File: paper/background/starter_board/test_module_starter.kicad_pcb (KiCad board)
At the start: 2 copper layers, 82.3 x 112.9 mm, 14 parts, among them J1 Barrel_Jack_12V, M1 ERM_Motor, M2 Stepper_4wire, M3 Servo_3pin, U1 D24V22F5_Buck, U2 Pi_Pico_W, U3 DRV2605L_Breakout, U4 DRV8871_Breakout, U5 Tic_T500

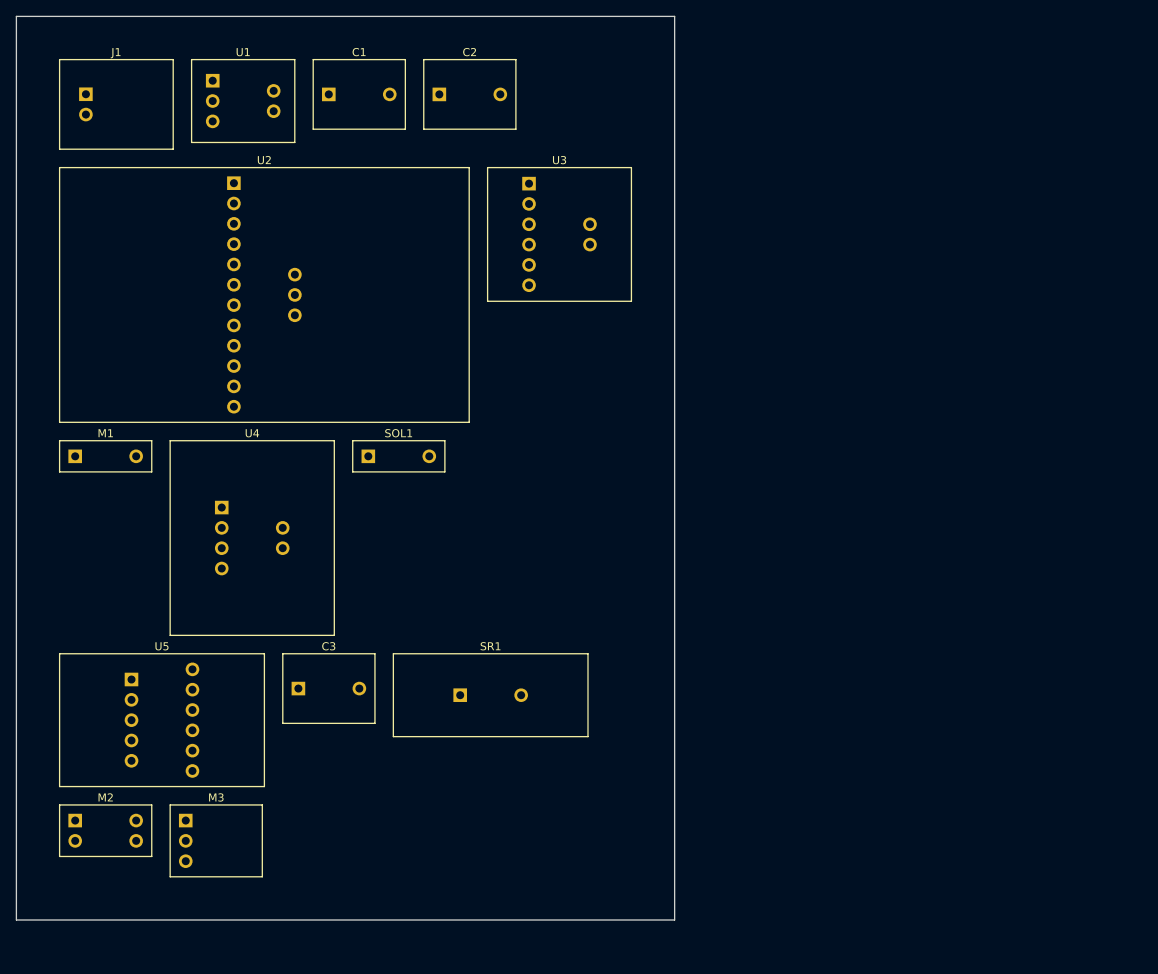
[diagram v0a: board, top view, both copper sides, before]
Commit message: Fix starter-board pin counts to match real parts (Pico W 15→40, etc.)
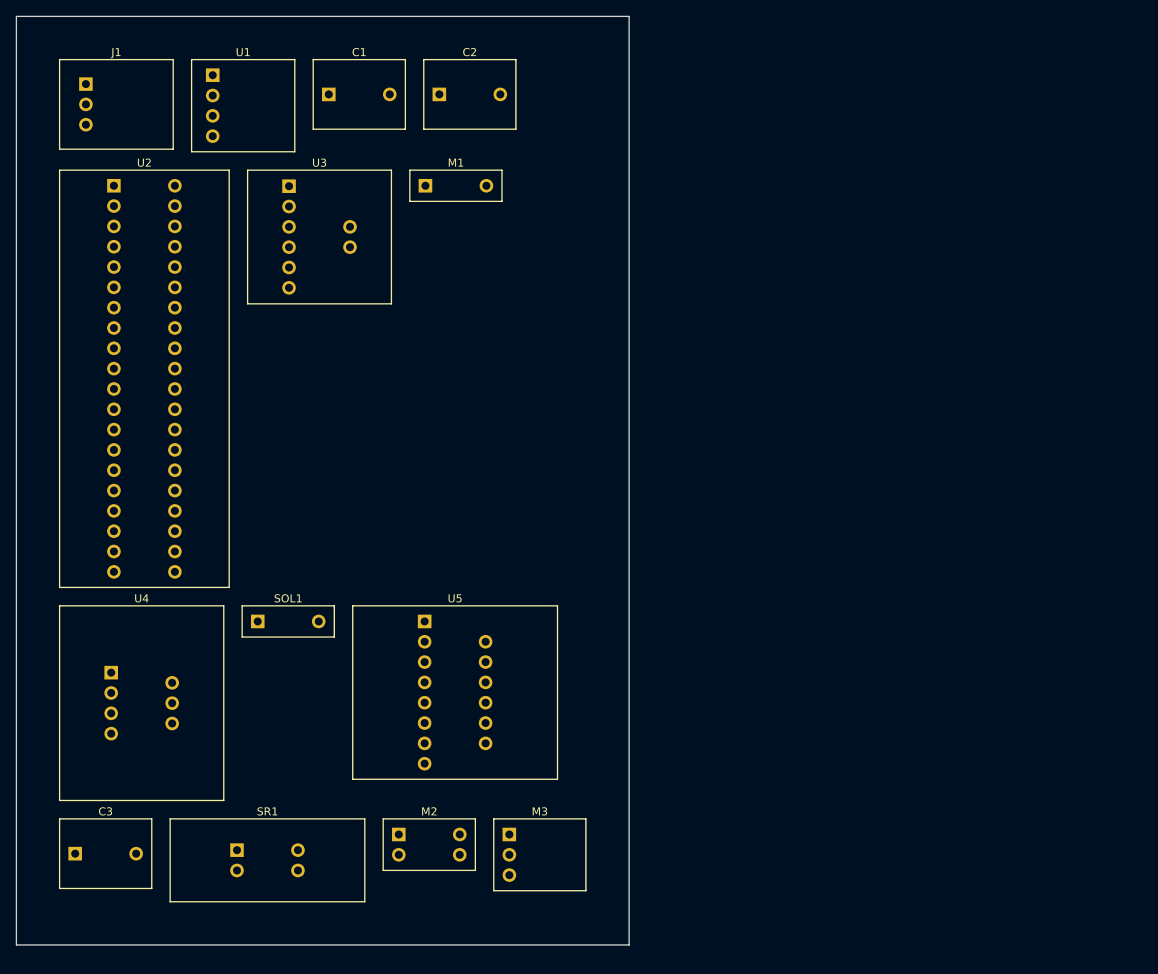
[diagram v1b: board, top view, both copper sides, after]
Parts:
- moved M1 55.3 mm to (49.9, 16.2)
- moved M2 40.5 mm to (46.6, 98.5)
- moved M3 40.5 mm to (60.4, 99.8)
- moved U5 36.8 mm to (49.8, 79.5)
- moved C3 34.7 mm to (6.16, 99.7)
- moved SR1 34.7 mm to (26.4, 100.5)
- moved U3 30.0 mm to (32.9, 22.6)
- moved U4 24.8 mm to (10.7, 80.8)
- moved SOL1 24.8 mm to (29.0, 70.6)
- moved U2 18.3 mm to (11.0, 40.3)
- moved U1 0.58 mm to (23.4, 6.16)
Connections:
- SR1 pad 2: GND -> +12V
- U1 pad 3: +12V -> +5V
- U1 pad 4: +5V -> +12V
- U2 pad 10: SOL_IN2 -> (no net)
- U2 pad 11: HAPT_EN -> (no net)
- U2 pad 12: SERVO_SIG -> (no net)
- U2 pad 13: +5V -> GND
- U2 pad 14: GND -> SOL_IN1
- U2 pad 15: +3V3 -> SOL_IN2
- U2 pad 3: (no net) -> GND
- U2 pad 5: STP_TX -> (no net)
- U2 pad 6: STP_RX -> STP_TX
- U2 pad 7: (no net) -> STP_RX
- U2 pad 8: (no net) -> GND
- U2 pad 9: SOL_IN1 -> (no net)
- U4 pad 3: SOL_IN1 -> SOL_A
- U4 pad 4: SOL_IN2 -> SOL_B
- U4 pad 5: SOL_A -> SOL_IN1
- U4 pad 6: SOL_B -> SOL_IN2
- U5 pad 10: STP_B1 -> GND
- U5 pad 11: STP_B2 -> STP_A1
- U5 pad 6: +12V -> (no net)
- U5 pad 8: STP_A1 -> (no net)
- U5 pad 9: STP_A2 -> +12V
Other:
- board size 82.3 x 112.9 mm -> 76.6 x 116.1 mm

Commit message: Swap starter-board placeholder pads for real KiCad library footprints
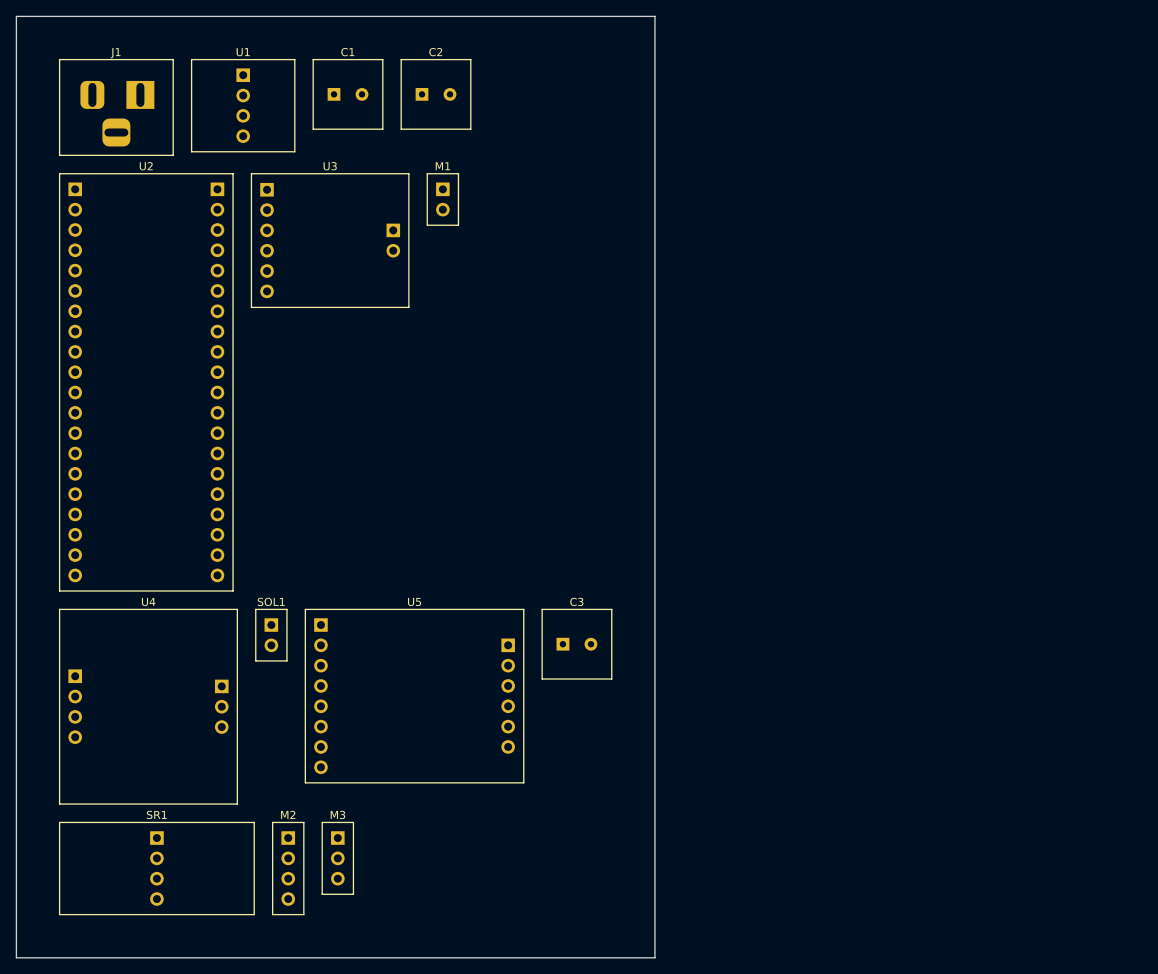
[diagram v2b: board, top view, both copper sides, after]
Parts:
- C1, C2, C3: footprint powder_doser_parts:Cap_Polar -> Capacitor_THT:CP_Radial_D8.0mm_P3.50mm
- J1: footprint powder_doser_parts:Barrel_Jack_12V -> Connector_BarrelJack:BarrelJack_Horizontal
- M1: footprint powder_doser_parts:ERM_Motor -> Connector_PinHeader_2.54mm:PinHeader_1x02_P2.54mm_Vertical
- M2: footprint powder_doser_parts:Stepper_4wire -> Connector_PinHeader_2.54mm:PinHeader_1x04_P2.54mm_Vertical
- M3: footprint powder_doser_parts:Servo_3pin -> Connector_PinHeader_2.54mm:PinHeader_1x03_P2.54mm_Vertical
- SOL1: footprint powder_doser_parts:Solenoid -> Connector_PinHeader_2.54mm:PinHeader_1x02_P2.54mm_Vertical
- moved C3 64.5 mm to (65.1, 73.5)
- moved M3 25.3 mm to (35.2, 100.2)
- moved M2 17.9 mm to (29.0, 101.5)
- moved SR1 13.9 mm to (12.6, 101.5)
- moved U5 5.09 mm to (44.8, 80.0)
- moved C2 4.23 mm to (47.5, 4.75)
- moved SOL1 2.72 mm to (26.9, 72.3)
- moved M1 2.37 mm to (48.3, 17.9)
- moved C1 1.41 mm to (36.5, 4.75)
- moved U3 1.40 mm to (34.2, 23.0)
- moved U4 0.96 mm to (11.5, 81.3)
- moved U2 0.51 mm to (11.2, 40.7)
- moved J1 0.38 mm to (7.50, 6.38)
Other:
- board size 76.6 x 116.1 mm -> 79.8 x 117.7 mm

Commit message: Implement Edison feedback: domain/cluster/edge-aware board placement
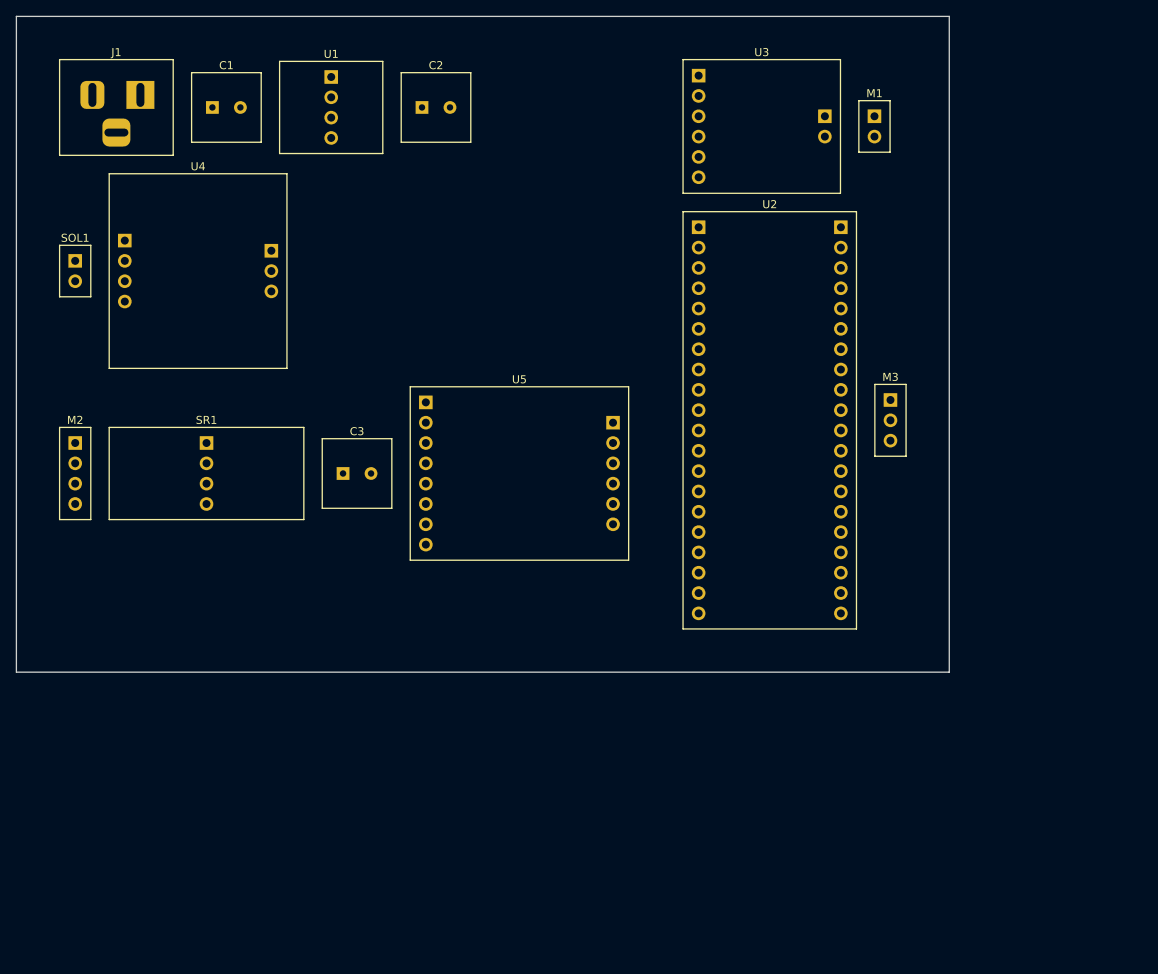
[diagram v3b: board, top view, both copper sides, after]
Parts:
- moved M3 88.1 mm to (104.3, 45.5)
- moved U2 78.1 mm to (89.2, 45.5)
- moved M2 56.1 mm to (2.35, 52.1)
- moved U3 55.8 mm to (88.2, 8.76)
- moved U4 54.8 mm to (17.7, 26.8)
- moved M1 54.7 mm to (102.3, 8.76)
- moved SOL1 51.7 mm to (2.35, 26.8)
- moved SR1 49.8 mm to (18.8, 52.1)
- moved C3 34.8 mm to (37.6, 52.1)
- moved U5 30.8 mm to (57.9, 52.1)
- moved C1 15.3 mm to (21.2, 6.38)
- moved U1 11.0 mm to (34.4, 6.38)
- moved C2 1.63 mm to (47.5, 6.38)
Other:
- board size 79.8 x 117.7 mm -> 116.6 x 82 mm
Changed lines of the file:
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@@
   )
   (footprint "powder_doser_parts:D24V22F5_Buck" (version 20221018) (generator kiutils) (layer "F.Cu")
-    (at 23.35 6.16 0)
+    (at 34.35 6.383333333333334 0)
     (descr "Powder-doser starter-board part; real land pattern(s): Connector_PinHeader_2.54mm:PinHeader_1x04_P2.54mm_Vertical")
     (fp_text reference "U1" (at 0 -6.66 0) (layer "F.SilkS")
@@
   )
   (footprint "Capacitor_THT:CP_Radial_D8.0mm_P3.50mm" (version 20221018) (generator kiutils) (layer "F.Cu")
-    (at 36.45 4.75 0)
+    (at 21.25 6.383333333333334 0)
     (descr "Powder-doser starter-board part; real land pattern(s): Capacitor_THT:CP_Radial_D8.0mm_P3.50mm")
     (fp_text reference "C1" (at 0 -5.25 0) (layer "F.SilkS")
@@
   )
   (footprint "Capacitor_THT:CP_Radial_D8.0mm_P3.50mm" (version 20221018) (generator kiutils) (layer "F.Cu")
-    (at 47.45 4.75 0)
+    (at 47.45 6.383333333333334 0)
     (descr "Powder-doser starter-board part; real land pattern(s): Capacitor_THT:CP_Radial_D8.0mm_P3.50mm")
     (fp_text reference "C2" (at 0 -5.25 0) (layer "F.SilkS")
@@
   )
   (footprint "powder_doser_parts:Pi_Pico_W" (version 20221018) (generator kiutils) (layer "F.Cu")
-    (at 11.24 40.74666666666667 0)
+    (at 89.16999999999999 45.49000000000001 0)
     (descr "Powder-doser starter-board part; real land pattern(s): Connector_PinHeader_2.54mm:PinHeader_1x20_P2.54mm_Vertical")
     (fp_text reference "U2" (at 0 -26.980000000000004 0) (layer "F.SilkS")
@@
   )
   (footprint "powder_doser_parts:DRV2605L_Breakout" (version 20221018) (generator kiutils) (layer "F.Cu")
-    (at 34.22 23.02166666666667 0)
+    (at 88.16999999999999 8.755 0)
     (descr "Powder-doser starter-board part; real land pattern(s): Connector_PinHeader_2.54mm:PinHeader_1x02_P2.54mm_Vertical, Connector_PinHeader_2.54mm:PinHeader_1x06_P2.54mm_Vertical")
     (fp_text reference "U3" (at 0 -9.255 0) (layer "F.SilkS")
@@
   )
   (footprint "Connector_PinHeader_2.54mm:PinHeader_1x02_P2.54mm_Vertical" (version 20221018) (generator kiutils) (layer "F.Cu")
-    (at 48.31 17.886666666666667 0)
+    (at 102.25999999999999 8.755 0)
     (descr "Powder-doser starter-board part; real land pattern(s): Connector_PinHeader_2.54mm:PinHeader_1x02_P2.54mm_Vertical")
     (fp_text reference "M1" (at 0 -4.12 0) (layer "F.SilkS")
@@
   )
   (footprint "powder_doser_parts:DRV8871_Breakout" (version 20221018) (generator kiutils) (layer "F.Cu")
-    (at 11.51 81.29166666666667 0)
+    (at 17.71 26.831666666666667 0)
     (descr "Powder-doser starter-board part; real land pattern(s): Connector_PinHeader_2.54mm:PinHeader_1x03_P2.54mm_Vertical, Connector_PinHeader_2.54mm:PinHeader_1x04_P2.54mm_Vertical")
     (fp_text reference "U4" (at 0 -13.065 0) (layer "F.SilkS")
@@
   )
   (footprint "Connector_PinHeader_2.54mm:PinHeader_1x02_P2.54mm_Vertical" (version 20221018) (generator kiutils) (layer "F.Cu")
-    (at 26.87 72.34666666666668 0)
+    (at 2.35 26.831666666666667 0)
     (descr "Powder-doser starter-board part; real land pattern(s): Connector_PinHeader_2.54mm:PinHeader_1x02_P2.54mm_Vertical")
     (fp_text reference "SOL1" (at 0 -4.12 0) (layer "F.SilkS")
@@
   )
   (footprint "powder_doser_parts:Tic_T500" (version 20221018) (generator kiutils) (layer "F.Cu")
-    (at 44.769999999999996 79.96666666666667 0)
+    (at 57.879999999999995 52.13666666666667 0)
     (descr "Powder-doser starter-board part; real land pattern(s): Connector_PinHeader_2.54mm:PinHeader_1x06_P2.54mm_Vertical, Connector_PinHeader_2.54mm:PinHeader_1x08_P2.54mm_Vertical")
     (fp_text reference "U5" (at 0 -11.74 0) (layer "F.SilkS")
@@
   )
   (footprint "Capacitor_THT:CP_Radial_D8.0mm_P3.50mm" (version 20221018) (generator kiutils) (layer "F.Cu")
-    (at 65.07 73.47666666666667 0)
+    (at 37.58 52.13666666666667 0)
     (descr "Powder-doser starter-board part; real land pattern(s): Capacitor_THT:CP_Radial_D8.0mm_P3.50mm")
     (fp_text reference "C3" (at 0 -5.25 0) (layer "F.SilkS")
@@
   )
   (footprint "powder_doser_parts:Shunt_Regulator" (version 20221018) (generator kiutils) (layer "F.Cu")
-    (at 12.565 101.51666666666667 0)
+    (at 18.765 52.13666666666667 0)
     (descr "Powder-doser starter-board part; real land pattern(s): Connector_PinHeader_2.54mm:PinHeader_1x04_P2.54mm_Vertical")
     (fp_text reference "SR1" (at 0 -6.66 0) (layer "F.SilkS")
@@
   )
   (footprint "Connector_PinHeader_2.54mm:PinHeader_1x04_P2.54mm_Vertical" (version 20221018) (generator kiutils) (layer "F.Cu")
-    (at 28.98 101.51666666666667 0)
+    (at 2.35 52.13666666666667 0)
     (descr "Powder-doser starter-board part; real land pattern(s): Connector_PinHeader_2.54mm:PinHeader_1x04_P2.54mm_Vertical")
     (fp_text reference "M2" (at 0 -6.66 0) (layer "F.SilkS")
@@
   )
   (footprint "Connector_PinHeader_2.54mm:PinHeader_1x03_P2.54mm_Vertical" (version 20221018) (generator kiutils) (layer "F.Cu")
-    (at 35.18 100.24666666666667 0)
+    (at 104.25999999999999 45.49000000000001 0)
     (descr "Powder-doser starter-board part; real land pattern(s): Connector_PinHeader_2.54mm:PinHeader_1x03_P2.54mm_Vertical")
     (fp_text reference "M3" (at 0 -5.390000000000001 0) (layer "F.SilkS")
@@
     )
   )
-  (gr_line (start -5.0 -5.0) (end 74.82 -5.0) (layer "Edge.Cuts") (width 0.1))
-  (gr_line (start 74.82 -5.0) (end 74.82 112.67666666666666) (layer "Edge.Cuts") (width 0.1))
-  (gr_line (start 74.82 112.67666666666666) (end -5.0 112.67666666666666) (layer "Edge.Cuts") (width 0.1))
-  (gr_line (start -5.0 112.67666666666666) (end -5.0 -5.0) (layer "Edge.Cuts") (width 0.1))
+  (gr_line (start -5.0 -5.0) (end 111.60999999999999 -5.0) (layer "Edge.Cuts") (width 0.1))
+  (gr_line (start 111.60999999999999 -5.0) (end 111.60999999999999 76.97000000000001) (layer "Edge.Cuts") (width 0.1))
+  (gr_line (start 111.60999999999999 76.97000000000001) (end -5.0 76.97000000000001) (layer "Edge.Cuts") (width 0.1))
+  (gr_line (start -5.0 76.97000000000001) (end -5.0 -5.0) (layer "Edge.Cuts") (width 0.1))
 )

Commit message: Add Waveshare Pico-2CH-RS232 module footprint for scale integration
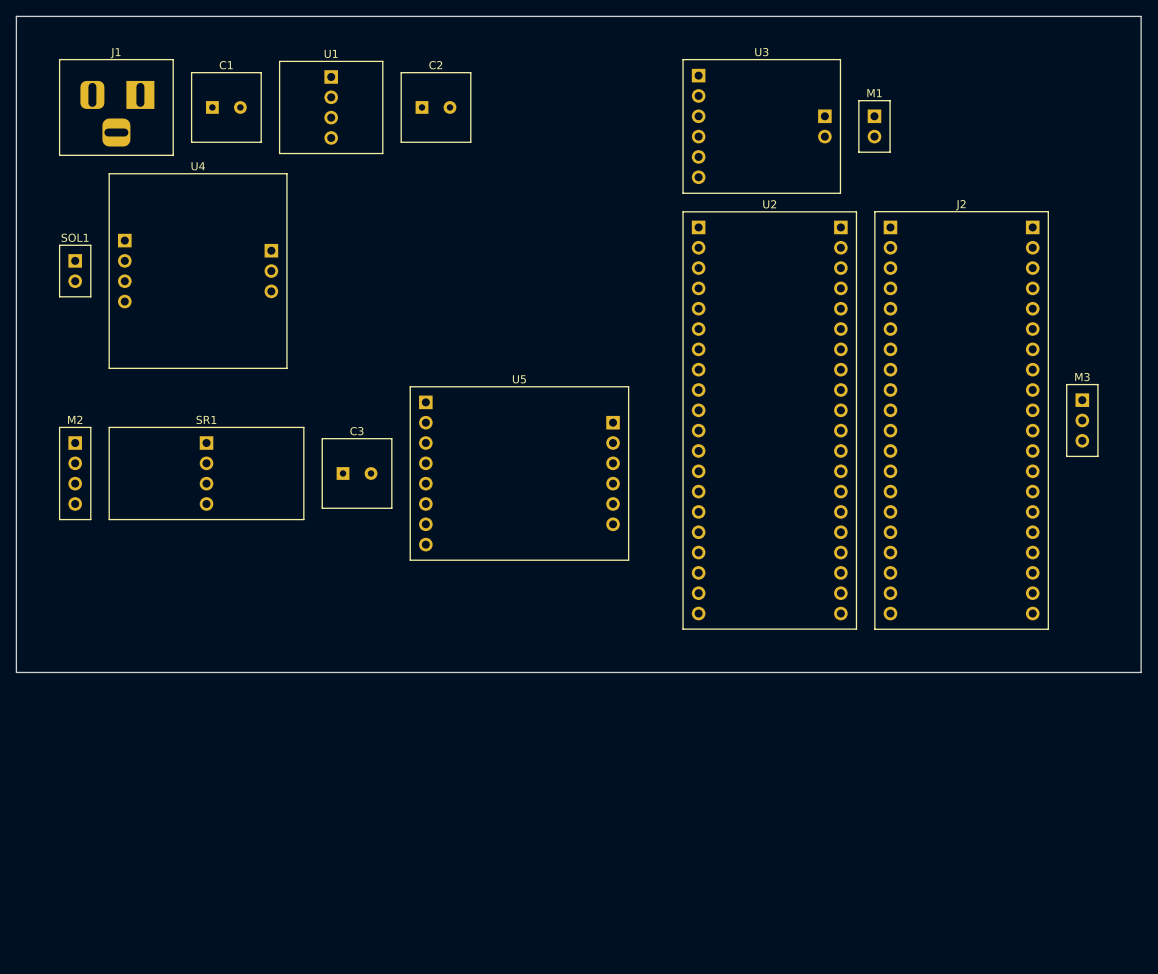
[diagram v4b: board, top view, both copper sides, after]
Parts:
- added J2: RS232_2CH_Module, powder_doser_parts:RS232_2CH_Module, F.Cu at (113.1, 45.5)
- moved M3 24.0 mm to (128.2, 45.5)
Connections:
- U2 pad 11: (no net) -> RS232_1_TXD
- U2 pad 12: (no net) -> RS232_1_RXD
- U2 pad 16: (no net) -> RS232_0_TXD
- U2 pad 17: (no net) -> RS232_0_RXD
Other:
- board size 116.6 x 82 mm -> 140.6 x 82 mm
